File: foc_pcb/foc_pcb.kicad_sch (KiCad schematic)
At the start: 38 parts, among them IC1 AS5600-ASOT, J1 IMU, J2 BATT_IN, J3 Conn_01x03, J4 power_supply, J5 ESP, U1 DRV8313PWPR

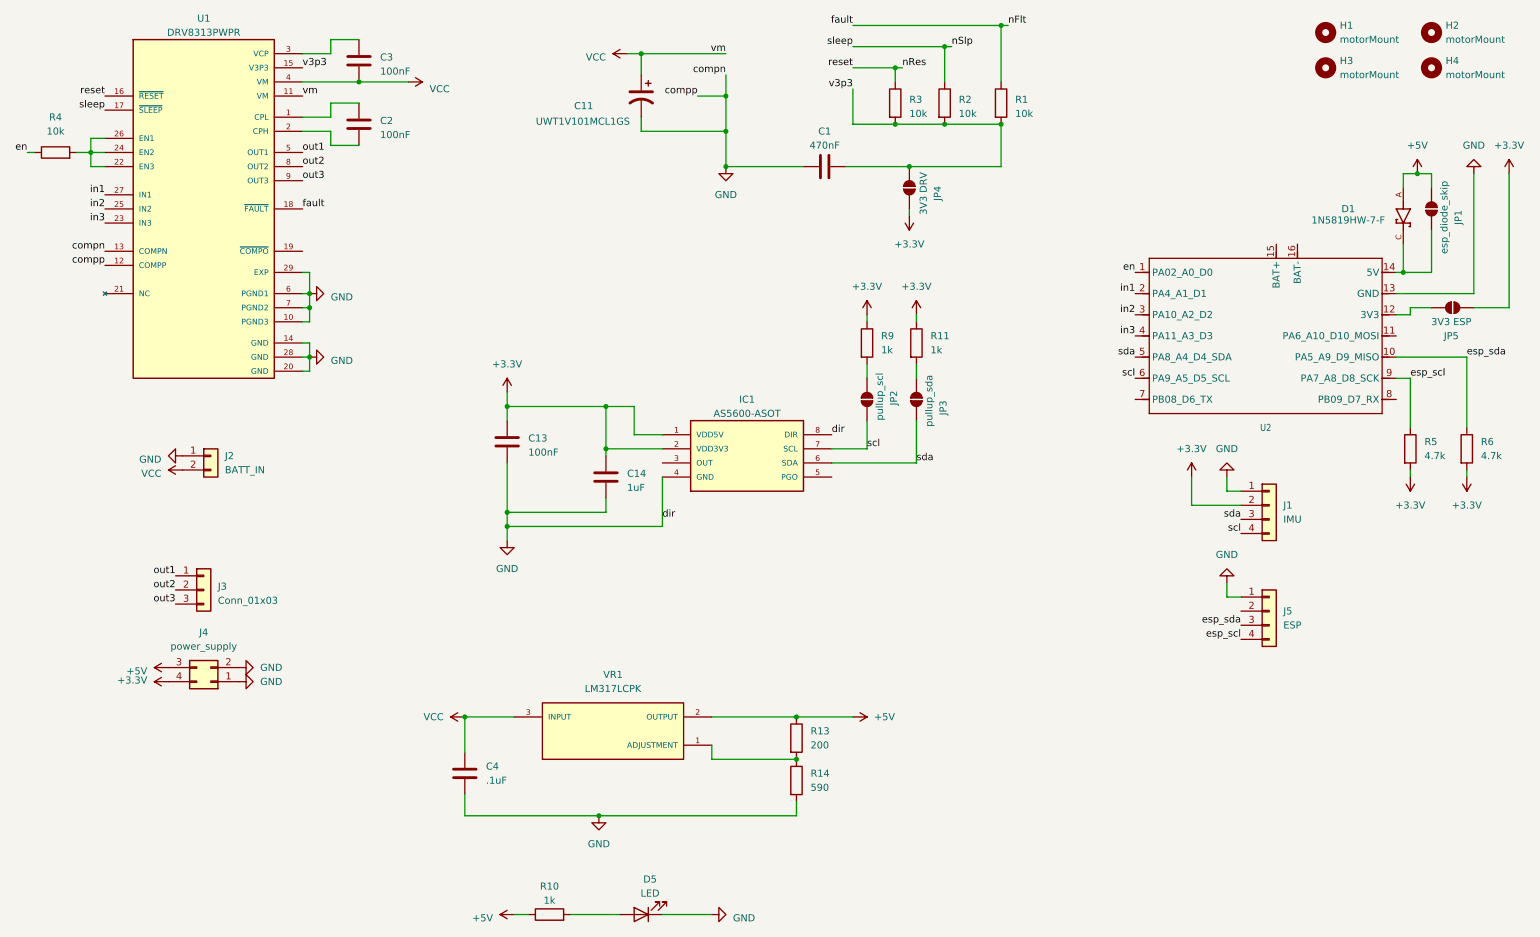
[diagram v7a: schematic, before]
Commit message: removed rendunant solder jumpers
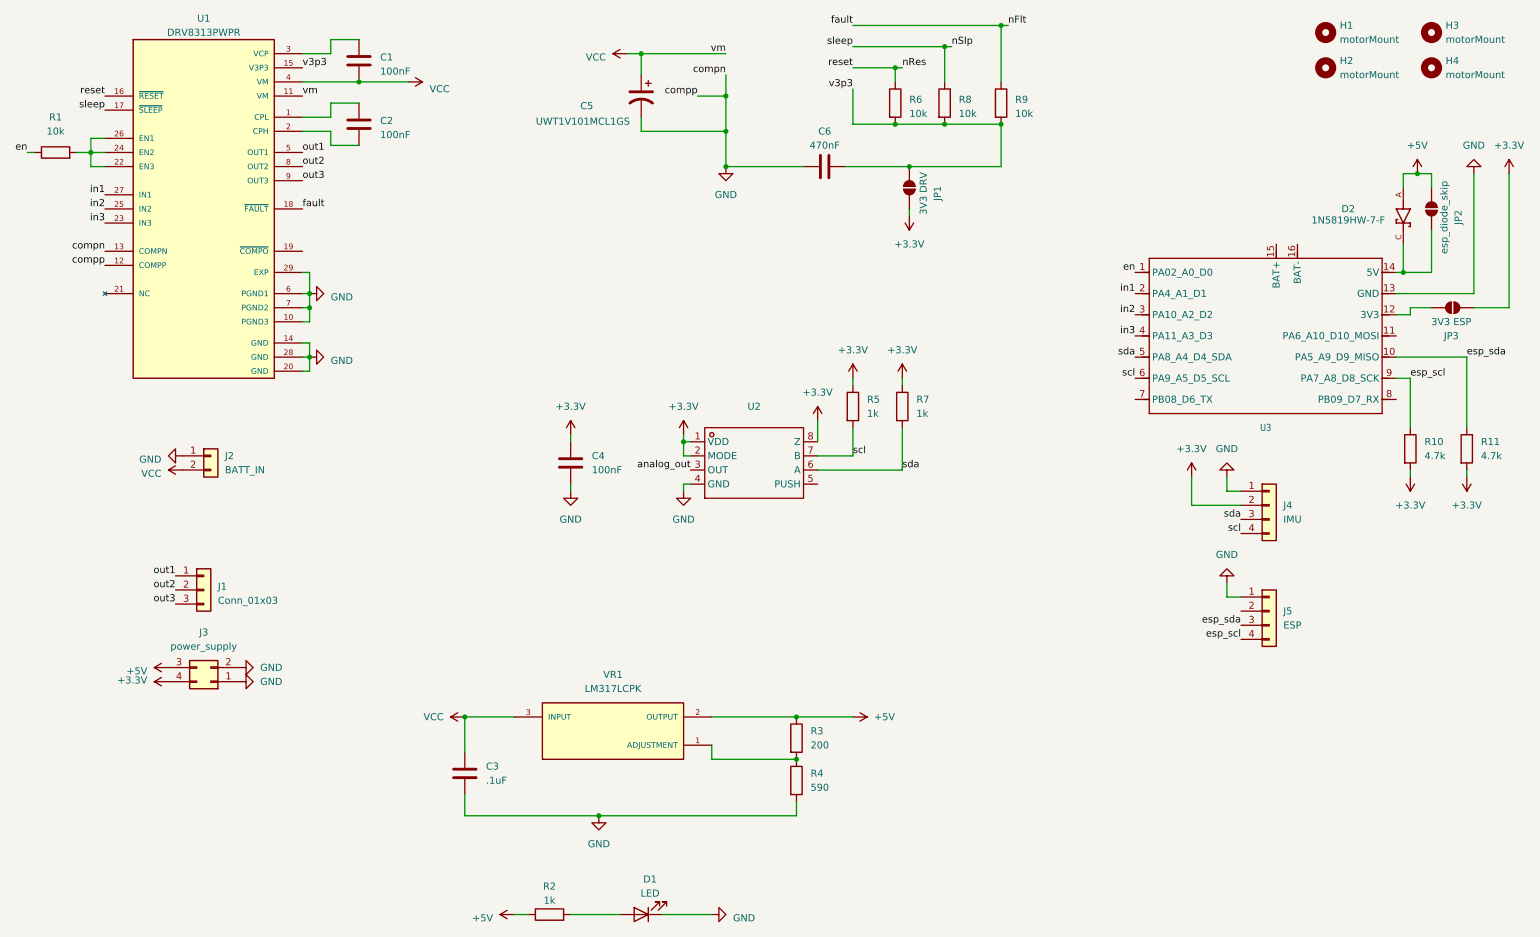
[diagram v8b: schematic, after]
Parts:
- removed C14: 1uF, Capacitor_SMD:C_0603_1608Metric, symbol Device:C
- removed IC1: AS5600-ASOT, AS5600-ASOT:SOIC127P600X175-8N, symbol AS5600-ASOT:AS5600-ASOT
- removed JP2: pullup_scl, Jumper:SolderJumper-2_P1.3mm_Open_TrianglePad1.0x1.5mm, symbol Jumper:SolderJumper_2_Open
- removed JP3: pullup_sda, Jumper:SolderJumper-2_P1.3mm_Open_TrianglePad1.0x1.5mm, symbol Jumper:SolderJumper_2_Open
- added U2: ~, MT6701CT-STD:SOP-8_L4.9-W3.9-P1.27-LS6.0-BL, symbol MT6701CT-STD:MT6701CT-STD
- renumbered C3 to C1, C4 to C3, C13 to C4, C11 to C5, C1 to C6, D5 to D1, D1 to D2, H3 to H2, H2 to H3, J3 to J1, J4 to J3, J1 to J4, JP4 to JP1, JP1 to JP2, JP5 to JP3, R4 to R1, R5 to R10, R6 to R11, R10 to R2, R13 to R3, R14 to R4, R9 to R5, R3 to R6, R11 to R7, R2 to R8, R1 to R9, U2 to U3
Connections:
- net +3.3V: now also C4.2, U2.1 (VDD), U2.2 (MODE), U2.8 (Z); no longer C4.1
- net GND: now also C4.1, U2.4 (GND); no longer C4.2
- net scl: now also R5.2, U2.7 (B)
- net sda: now also R7.2, U2.6 (A)
- new net analog_out: U2.3 (OUT)
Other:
- moved on the sheet: C4, R5, R7
